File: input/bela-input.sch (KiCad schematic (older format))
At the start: 57 parts, among them P1 MTA-156-4, P2 in_modular, P3 out_bela, U1 TL074, U2 TL074, U3 TL071

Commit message: major updates! nearly done with input
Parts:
- removed P2: in_modular, symbol CONN_01X04
- removed P3: out_bela, symbol CONN_01X04
- removed VR1: 10k, symbol VR
- added C11, C12, C13, C14, C15, C16: 10n, Capacitors_ThroughHole:C_Rect_L4_W2.5_P2.5, symbol C
- added P2: in_modular, Pin_Headers:Pin_Header_Straight_2x04, symbol CONN_02X04
- added P3: out_bela, Pin_Headers:Pin_Header_Straight_2x04, symbol CONN_02X04
- added TR1: TRIM, trim:trimmer, symbol TRIM
- C1, C2, C3, C4, C5, C6, C7, C8, Cci1, Cci2, Cci3, Cci4: footprint (none) -> Capacitors_ThroughHole:C_Rect_L4_W2.5_P2.5
- R1, R10, R11, R12, R13, R14, R15, R16, R17, R18, R19, R2, R20, R21, R22, R23, R24, R25, R26, R27, R28, R29, R3, R30, R31, R32, R33, R4, R5, R6, R7, R8, R9, RinF1: footprint (none) -> Resistors_ThroughHole:Resistor_Vertical_RM5mm
- U1, U2: footprint (none) -> Housings_DIP:DIP-14_W7.62mm_LongPads
- U3: footprint (none) -> Housings_DIP:DIP-8_W7.62mm_LongPads
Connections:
- net GND: now also C11.2, C12.1, C13.2, C14.1, C15.2, C16.1, P2.2 (P2), P2.4 (P4), P2.6 (P6), P2.8 (P8), P3.1 (P1), P3.3 (P3), P3.5 (P5), P3.7 (P7)
- net VCC: now also R34.1, C11.1, C13.1, C15.1; no longer R34.2
- net VSS: now also R35.2, C12.2, C14.2, C16.2, TR1.1; no longer R35.1
- net bela_ain0: now also P3.2 (P2)
- net bela_ain1: now also P3.4 (P4)
- net bela_ain2: now also P3.6 (P6)
- net bela_ain3: now also P3.8 (P8)
- net modular_ain0: now also P2.1 (P1)
- net modular_ain1: now also P2.3 (P3)
- net modular_ain2: now also P2.5 (P5)
- net modular_ain3: now also P2.7 (P7)
- net at R5.1: now also R9.2; no longer R9.1
- net at R13.2, U1.2 (-): now also R9.1; no longer R9.2
- net at R6.1: now also R10.2; no longer R10.1
- net at R14.2, U1.6 (-): now also R10.1; no longer R10.2
- net at R7.1: now also R11.2; no longer R11.1
- net at R15.2, U2.2 (-): now also R11.1; no longer R11.2
- net at R8.1: now also R12.2; no longer R12.1
- net at R16.2, U2.6 (-): now also R12.1; no longer R12.2
- net at RinF1.1: now also TR1.2, TR1.3
- net at P1.1 (P1): now also R34.2; no longer R34.1
- net at P1.4 (P4): now also R35.1; no longer R35.2
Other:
- note added: "decoupling caps"

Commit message: relayout of input
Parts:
- R1, R10, R11, R12, R13, R14, R15, R16, R17, R18, R19, R2, R20, R21, R22, R23, R24, R25, R26, R27, R28, R29, R3, R30, R31, R32, R33, R4, R5, R6, R7, R8, R9, RinF1: footprint Resistors_ThroughHole:Resistor_Vertical_RM5mm -> xnorman:Resistor_Horizontal_RM10mm-xnorman
- R34, R35: footprint Resistors_ThroughHole:Resistor_Vertical_RM5mm -> xnorman:Resistor_Vertical_RM5mm-xnor

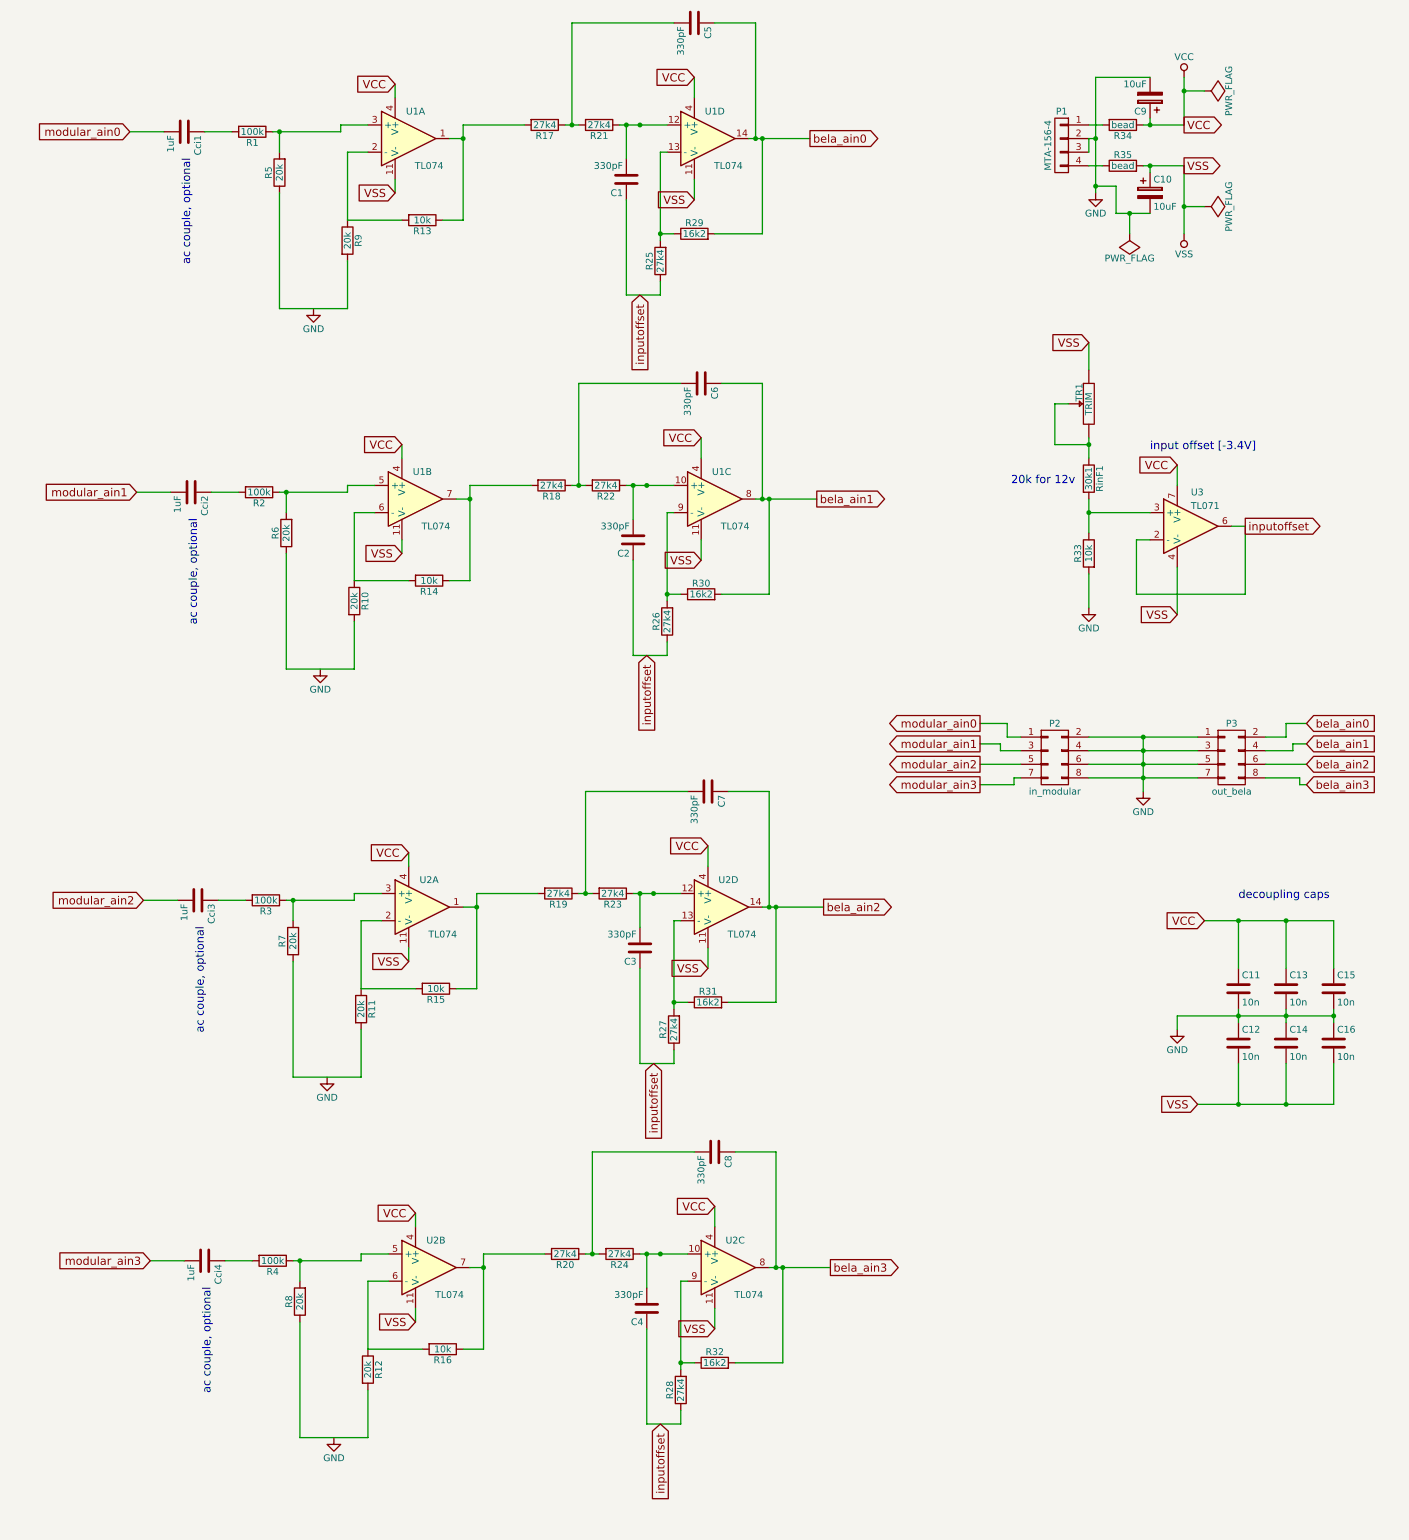
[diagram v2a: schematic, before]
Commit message: oops, forgot to connect the grounds
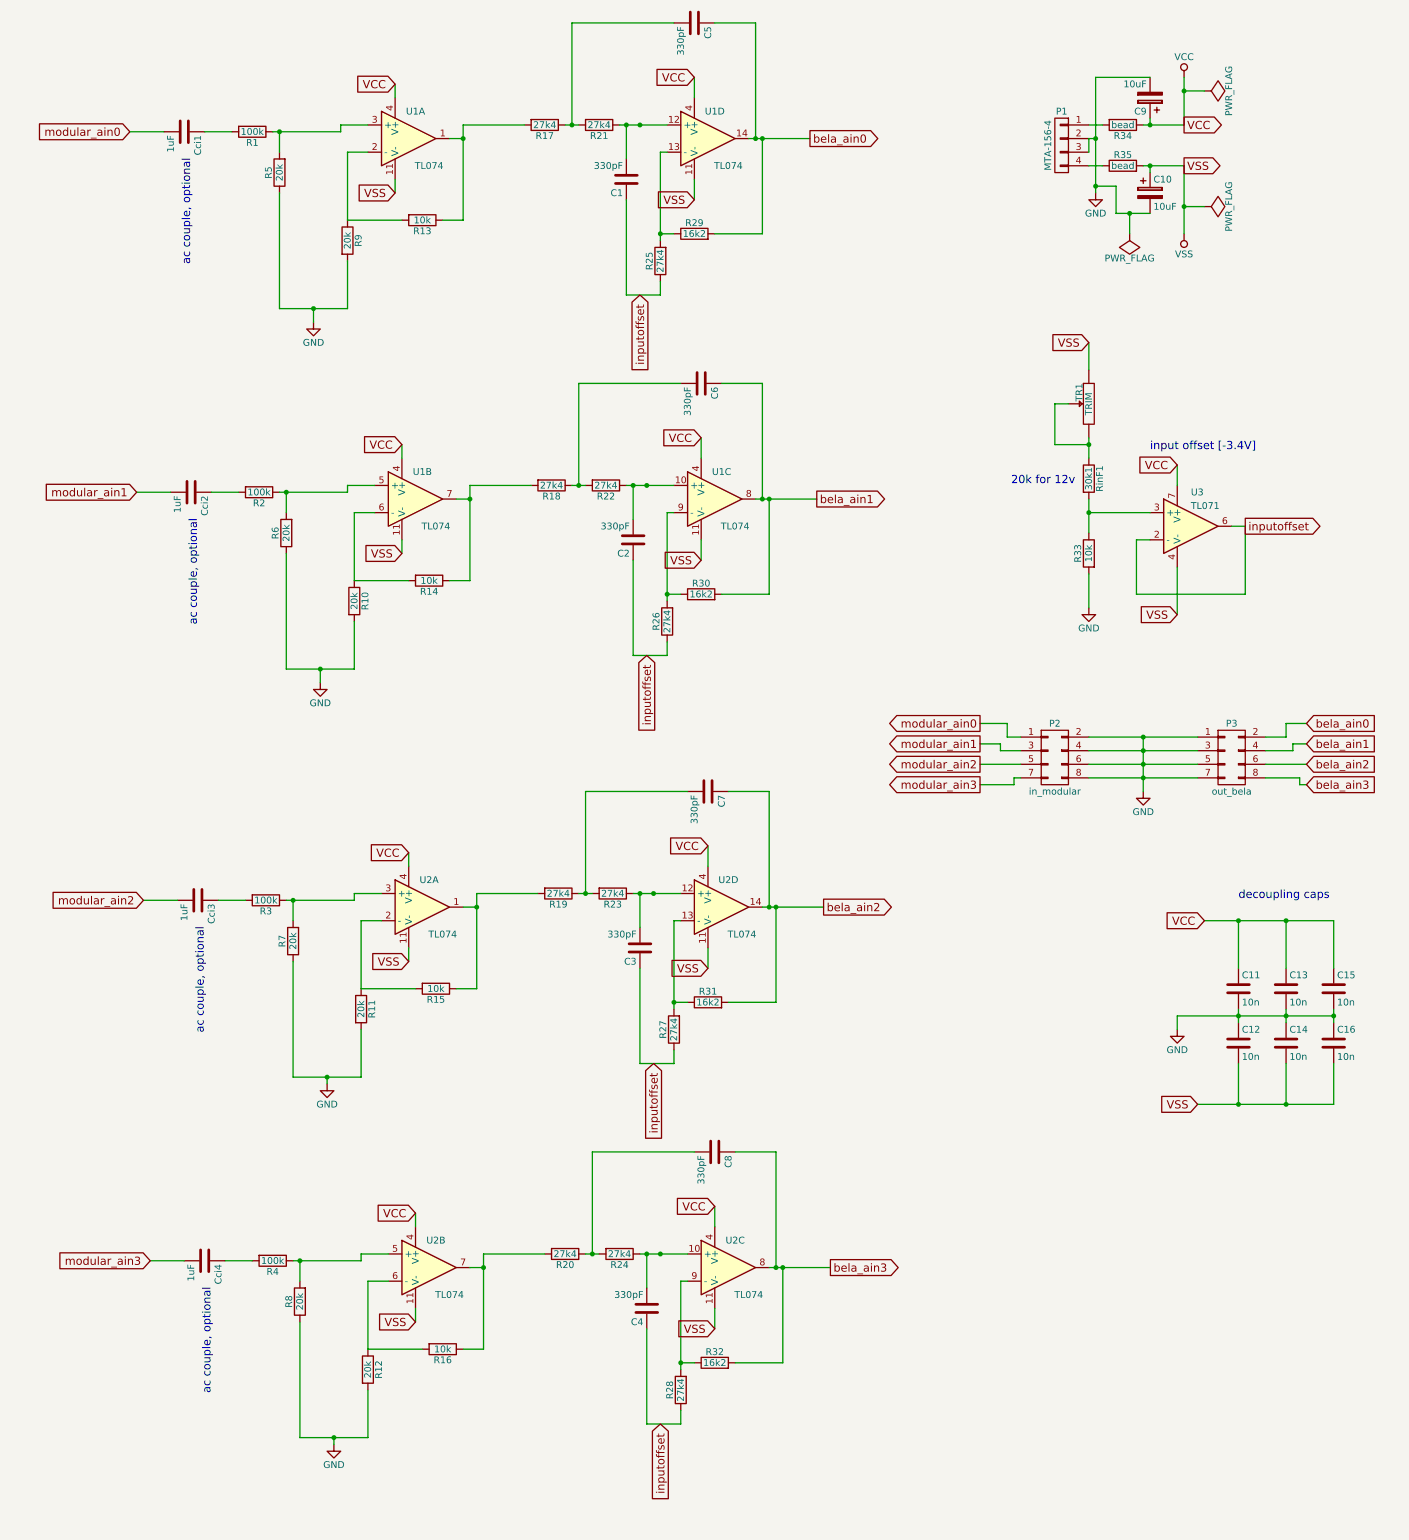
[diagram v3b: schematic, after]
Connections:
- net GND: now also R10.2, R11.2, R12.2, R5.1, R6.1, R7.1, R8.1, R9.2
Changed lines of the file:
@@
 L GND #PWR01
 U 1 1 5844A24C
-P 2850 3200
-F 0 "#PWR01" H 2850 2950 50  0001 C CNN
-F 1 "GND" H 2850 3050 50  0000 C CNN
-F 2 "" H 2850 3200 50  0000 C CNN
-F 3 "" H 2850 3200 50  0000 C CNN
-	1    2850 3200
+P 2850 3300
+F 0 "#PWR01" H 2850 3050 50  0001 C CNN
+F 1 "GND" H 2850 3150 50  0000 C CNN
+F 2 "" H 2850 3300 50  0000 C CNN
+F 3 "" H 2850 3300 50  0000 C CNN
+	1    2850 3300
 	1    0    0    -1
 $EndComp
@@
 L GND #PWR02
 U 1 1 5844A2E1
-P 2900 5850
-F 0 "#PWR02" H 2900 5600 50  0001 C CNN
-F 1 "GND" H 2900 5700 50  0000 C CNN
-F 2 "" H 2900 5850 50  0000 C CNN
-F 3 "" H 2900 5850 50  0000 C CNN
-	1    2900 5850
+P 2900 5950
+F 0 "#PWR02" H 2900 5700 50  0001 C CNN
+F 1 "GND" H 2900 5800 50  0000 C CNN
+F 2 "" H 2900 5950 50  0000 C CNN
+F 3 "" H 2900 5950 50  0000 C CNN
+	1    2900 5950
 	1    0    0    -1
 $EndComp
@@
 L GND #PWR03
 U 1 1 5844A376
-P 2950 8850
-F 0 "#PWR03" H 2950 8600 50  0001 C CNN
-F 1 "GND" H 2950 8700 50  0000 C CNN
-F 2 "" H 2950 8850 50  0000 C CNN
-F 3 "" H 2950 8850 50  0000 C CNN
-	1    2950 8850
+P 2950 8900
+F 0 "#PWR03" H 2950 8650 50  0001 C CNN
+F 1 "GND" H 2950 8750 50  0000 C CNN
+F 2 "" H 2950 8900 50  0000 C CNN
+F 3 "" H 2950 8900 50  0000 C CNN
+	1    2950 8900
 	1    0    0    -1
 $EndComp
@@
 L GND #PWR04
 U 1 1 5844A40B
-P 3000 11500
-F 0 "#PWR04" H 3000 11250 50  0001 C CNN
-F 1 "GND" H 3000 11350 50  0000 C CNN
-F 2 "" H 3000 11500 50  0000 C CNN
-F 3 "" H 3000 11500 50  0000 C CNN
-	1    3000 11500
+P 3000 11550
+F 0 "#PWR04" H 3000 11300 50  0001 C CNN
+F 1 "GND" H 3000 11400 50  0000 C CNN
+F 2 "" H 3000 11550 50  0000 C CNN
+F 3 "" H 3000 11550 50  0000 C CNN
+	1    3000 11550
 	1    0    0    -1
 $EndComp
@@
 	5800 2650 6150 2650
 Wire Wire Line
-	6150 2650 6150 1950
+	6150 1950 6150 2650
 Wire Wire Line
 	6050 1950 6500 1950
@@
 	5850 5300 6200 5300
 Wire Wire Line
-	6200 5300 6200 4600
+	6200 4600 6200 5300
 Wire Wire Line
 	6100 4600 6550 4600
@@
 	5900 8300 6250 8300
 Wire Wire Line
-	6250 8300 6250 7600
+	6250 7600 6250 8300
 Wire Wire Line
 	6150 7600 6600 7600
@@
 	5950 10950 6300 10950
 Wire Wire Line
-	6300 10950 6300 10250
+	6300 10250 6300 10950
 Wire Wire Line
 	6200 10250 6650 10250
@@
 	8300 4200 8550 4200
 Connection ~ 8550 4200
+Wire Wire Line
+	2850 3200 2850 3300
+Connection ~ 2850 3200
+Wire Wire Line
+	2900 5850 2900 5950
+Connection ~ 2900 5850
+Wire Wire Line
+	2950 8850 2950 8900
+Connection ~ 2950 8850
+Wire Wire Line
+	3000 11500 3000 11550
+Connection ~ 3000 11500
 $EndSCHEMATC
